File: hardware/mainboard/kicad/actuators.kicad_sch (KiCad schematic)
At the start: 14 parts, among them J5 J_SERVO1, J6 J_SERVO2, J7 J_SERVO3, J8 J_MOT, U7 DRV8833PWPR

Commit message: Platine rev B geroutet: alle 134 Footprints platziert, DRC ohne Fehler, 3 offene Verbindungen; Renders und Lagenbilder; Fertigervergleich
- Lagen: In1 GND, B.Cu geteilte Versorgungsflaeche GND_PWR/5V_SYS, Plane-Vias an jedem SMD-Pad
- Freerouting 2.5.0 (JAR, Temurin 25) mit zwei Nachlaeufen auf fixierter Verdrahtung und kollisionsgeprueften Stummeln
- check_design.py: Netzliste gegen Spezifikation §4 (OK), make.sh fuer die ganze Kette
- 3D-Modelle Teensy 4.1 und XT30PW-M (CadQuery), Renders und layers.pdf in kicad/img
- Fertiger_2026-10-21.md: JLCPCB empfohlen, Aisler als EU-Rueckfall, BMP390 bei JLC nicht lieferbar
- naechster Schritt laut kicad/README.md §8: Review-Punkte A1-A5 (review_kicad_2026-10-21.md) vor dem Handrouting

Co-Authored-By: Claude Opus 5.5 <noreply@anthropic.com>
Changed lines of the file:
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@@
 		(company "Mission Space")
 		(comment 1 "TVC-Servos am 2S-Akku, Fallschirm-Servo, Rollmotor DRV8833")
-		(comment 2 "erzeugt von hardware/mainboard/kicad/gen_schematic.py aus circuit.py - nicht von Hand aendern")
+		(comment 2 "erzeugt aus circuit.py (gen_schematic.py)")
 	)
 	(text "TVC-Servos am 2S-Akku, Fallschirm-Servo, Rollmotor DRV8833"
@@
 		(stroke (width 0) (type default))
 	)
-	(label "SERVO_YAW_S"
+	(global_label "SERVO_YAW_S"
+		(shape passive)
 		(at 26.67 64.77 270)
 		(fields_autoplaced yes)
-		(effects (font (size 1.27 1.27)) (justify right bottom))
+		(effects (font (size 1.27 1.27)) (justify right))
 	)
 	(symbol
@@
 		(stroke (width 0) (type default))
 	)
-	(label "SERVO_YAW_S"
+	(global_label "SERVO_YAW_S"
+		(shape passive)
 		(at 54.61 44.45 180)
 		(fields_autoplaced yes)
-		(effects (font (size 1.27 1.27)) (justify right bottom))
+		(effects (font (size 1.27 1.27)) (justify right))
 	)
 	(wire
@@
 		(stroke (width 0) (type default))
 	)
-	(label "SERVO_PITCH_S"
+	(global_label "SERVO_PITCH_S"
+		(shape passive)
 		(at 68.58 67.31 270)
 		(fields_autoplaced yes)
-		(effects (font (size 1.27 1.27)) (justify right bottom))
+		(effects (font (size 1.27 1.27)) (justify right))
 	)
 	(symbol
@@
 		(stroke (width 0) (type default))
 	)
-	(label "SERVO_PITCH_S"
+	(global_label "SERVO_PITCH_S"
+		(shape passive)
 		(at 99.06 44.45 180)
 		(fields_autoplaced yes)
-		(effects (font (size 1.27 1.27)) (justify right bottom))
+		(effects (font (size 1.27 1.27)) (justify right))
 	)
 	(wire
@@
 		(stroke (width 0) (type default))
 	)
-	(label "SERVO_CHUTE_S"
+	(global_label "SERVO_CHUTE_S"
+		(shape passive)
 		(at 114.3 67.31 270)
 		(fields_autoplaced yes)
-		(effects (font (size 1.27 1.27)) (justify right bottom))
+		(effects (font (size 1.27 1.27)) (justify right))
 	)
 	(symbol
@@
 		(stroke (width 0) (type default))
 	)
-	(label "SERVO_CHUTE_S"
+	(global_label "SERVO_CHUTE_S"
+		(shape passive)
 		(at 143.51 44.45 180)
 		(fields_autoplaced yes)
-		(effects (font (size 1.27 1.27)) (justify right bottom))
+		(effects (font (size 1.27 1.27)) (justify right))
 	)
 	(wire
@@
 		(stroke (width 0) (type default))
 	)
-	(label "U7_SLEEP"
+	(global_label "U7_SLEEP"
+		(shape passive)
 		(at 179.07 62.23 180)
 		(fields_autoplaced yes)
-		(effects (font (size 1.27 1.27)) (justify right bottom))
+		(effects (font (size 1.27 1.27)) (justify right))
 	)
 	(wire
@@
 		(stroke (width 0) (type default))
 	)
-	(label "MOT_A"
+	(global_label "MOT_A"
+		(shape passive)
 		(at 209.55 74.93 0)
 		(fields_autoplaced yes)
-		(effects (font (size 1.27 1.27)) (justify left bottom))
+		(effects (font (size 1.27 1.27)) (justify left))
 	)
 	(wire
@@
 		(stroke (width 0) (type default))
 	)
-	(label "MOT_B"
+	(global_label "MOT_B"
+		(shape passive)
 		(at 209.55 77.47 0)
 		(fields_autoplaced yes)
-		(effects (font (size 1.27 1.27)) (justify left bottom))
+		(effects (font (size 1.27 1.27)) (justify left))
 	)
 	(wire
@@
 		(stroke (width 0) (type default))
 	)
-	(label "MOT_B"
+	(global_label "MOT_B"
+		(shape passive)
 		(at 209.55 82.55 0)
 		(fields_autoplaced yes)
-		(effects (font (size 1.27 1.27)) (justify left bottom))
+		(effects (font (size 1.27 1.27)) (justify left))
 	)
 	(wire
@@
 		(stroke (width 0) (type default))
 	)
-	(label "MOT_A"
+	(global_label "MOT_A"
+		(shape passive)
 		(at 209.55 80.01 0)
 		(fields_autoplaced yes)
-		(effects (font (size 1.27 1.27)) (justify left bottom))
+		(effects (font (size 1.27 1.27)) (justify left))
 	)
 	(wire
@@
 		(stroke (width 0) (type default))
 	)
-	(label "U7_VCP"
+	(global_label "U7_VCP"
+		(shape passive)
 		(at 179.07 64.77 180)
 		(fields_autoplaced yes)
-		(effects (font (size 1.27 1.27)) (justify right bottom))
+		(effects (font (size 1.27 1.27)) (justify right))
 	)
 	(wire
@@
 		(stroke (width 0) (type default))
 	)
-	(label "U7_VINT"
+	(global_label "U7_VINT"
+		(shape passive)
 		(at 199.39 54.61 90)
 		(fields_autoplaced yes)
-		(effects (font (size 1.27 1.27)) (justify left bottom))
+		(effects (font (size 1.27 1.27)) (justify left))
 	)
 	(wire
@@
 		(stroke (width 0) (type default))
 	)
-	(label "U7_SLEEP"
+	(global_label "U7_SLEEP"
+		(shape passive)
 		(at 227.33 63.5 270)
 		(fields_autoplaced yes)
-		(effects (font (size 1.27 1.27)) (justify right bottom))
+		(effects (font (size 1.27 1.27)) (justify right))
 	)
 	(symbol
@@
 		(stroke (width 0) (type default))
 	)
-	(label "U7_VCP"
+	(global_label "U7_VCP"
+		(shape passive)
 		(at 294.64 48.26 90)
 		(fields_autoplaced yes)
-		(effects (font (size 1.27 1.27)) (justify left bottom))
+		(effects (font (size 1.27 1.27)) (justify left))
 	)
 	(wire
@@
 		(stroke (width 0) (type default))
 	)
-	(label "U7_VINT"
+	(global_label "U7_VINT"
+		(shape passive)
 		(at 170.18 115.57 90)
 		(fields_autoplaced yes)
-		(effects (font (size 1.27 1.27)) (justify left bottom))
+		(effects (font (size 1.27 1.27)) (justify left))
 	)
 	(wire
@@
 		(stroke (width 0) (type default))
 	)
-	(label "MOT_A"
+	(global_label "MOT_A"
+		(shape passive)
 		(at 191.77 109.22 180)
 		(fields_autoplaced yes)
-		(effects (font (size 1.27 1.27)) (justify right bottom))
+		(effects (font (size 1.27 1.27)) (justify right))
 	)
 	(wire
@@
 		(stroke (width 0) (type default))
 	)
-	(label "MOT_B"
+	(global_label "MOT_B"
+		(shape passive)
 		(at 191.77 111.76 180)
 		(fields_autoplaced yes)
-		(effects (font (size 1.27 1.27)) (justify right bottom))
+		(effects (font (size 1.27 1.27)) (justify right))
 	)
 	(rectangle
@@
 		(stroke (width 0) (type default))
 	)
-	(label "U7_VINT"
+	(global_label "U7_VINT"
+		(shape passive)
 		(at 318.77 44.45 270)
 		(fields_autoplaced yes)
-		(effects (font (size 1.27 1.27)) (justify right bottom))
+		(effects (font (size 1.27 1.27)) (justify right))
 	)
 	(embedded_fonts no)

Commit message: Kartonaut: Name, Missionsabzeichen, Bestückungsdruck neu, Lötstopp blau
- Projekt heißt Kartonaut (Karton + Astronaut); Flüge werden hochgezählt, Erstflug = Kartonaut 1
- Abzeichen als Polygone in hardware/mainboard/kicad/logo.py, SVGs in docs/brand/
- spacecode/ -> firmware/, Bodenstation-Repo groundcode -> kartonaut-ground (Links, .gitignore)
- gen_pcb.py silk: Bestückungsdruck nur neu setzen, auf der gerouteten Platine; 1,0 mm Schrift,
  freie Plätze statt Überlappungen, Kurznamen an den Steckern, Testpunkte mit Netznamen,
  kleines Abzeichen vorn; hinten Abzeichen 20 mm und Steckerbelegung
- Stackup JLC04161H-7628 mit blauem Lötstopp im Board, Renders mit Stackup-Farben
- DRC-Druckwarnungen 167 -> 14 (Rest aus Footprint-Umrissen)

Co-Authored-By: Claude Opus 5.5 <noreply@anthropic.com>
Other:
- company: Mission Space -> Kartonaut
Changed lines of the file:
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@@
 		(date "2026-10-21")
 		(rev "B")
-		(company "Mission Space")
+		(company "Kartonaut")
 		(comment 1 "TVC-Servos am 2S-Akku, Fallschirm-Servo, Rollmotor DRV8833")
 		(comment 2 "erzeugt aus circuit.py (gen_schematic.py)")

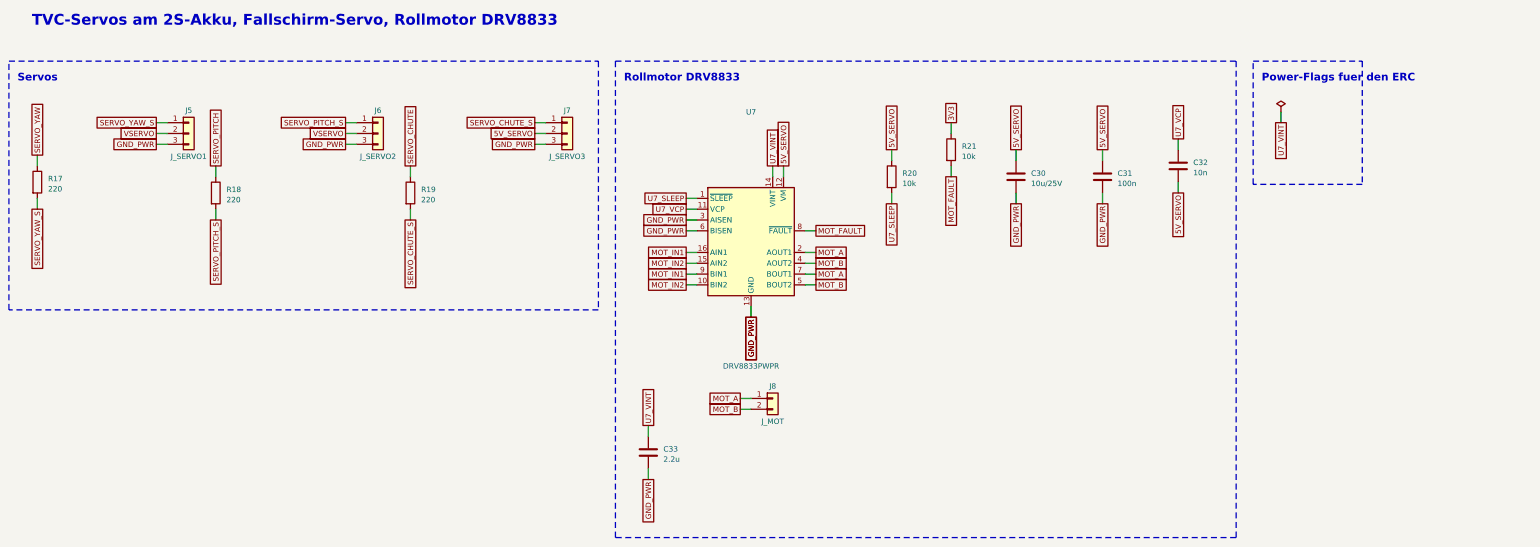
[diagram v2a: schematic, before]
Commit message: Mainboard rev B1: Review A1-A8 und Entscheidungen E1-E10 eingearbeitet, 2S-Pfad als F.Cu-Flaechen, 28 Verbindungen offen
Schaltung (circuit.py, ERC 0, Netzliste gegen README §4 OK): Hold-up hinter D1, EN-Teiler 330k/115k,
P-FET-Lastschalter je Akku, Polyfuse je Akku, Kelvin-Shunt mit INA239 an SPI1, BMP390 an SPI1,
74HC138/74HC4051 mit gemeinsamer Adresse, J_STACK 2x10 mit LDO 3V3_EXP, 1S-Lader MCP73831,
J_CHG2, vier Pyro-Kanaele (3/4 DNP), vierter Servo, alle Servos und Rollmotor an VSERVO,
3V3_SENS, eine WS2812B-Kette, Summer Pin 37, E22 NRST Pin 6; 166 Bauteile.

Platine (gen_pcb.py): neue Platzierung, 2S-Pfad, Pyro-Ausgaenge und VSYS_IN als F.Cu-Flaechen mit
Sperrflaechen fuer Freerouting, Strom-Klasse nur F.Cu, IMU-Zone 5 mm, patch mit Umweg ueber In2.
DRC 0 Fehler, Paritaet 0, kein 2S-Netz auf In2; 28 offene Verbindungen, Liste in kicad/README.md §5.5.
Spezifikation README.md und kicad/README.md auf B1 nachgezogen, review_check_layout.py fuer B1.

Co-Authored-By: Claude Opus 5.5 <noreply@anthropic.com>
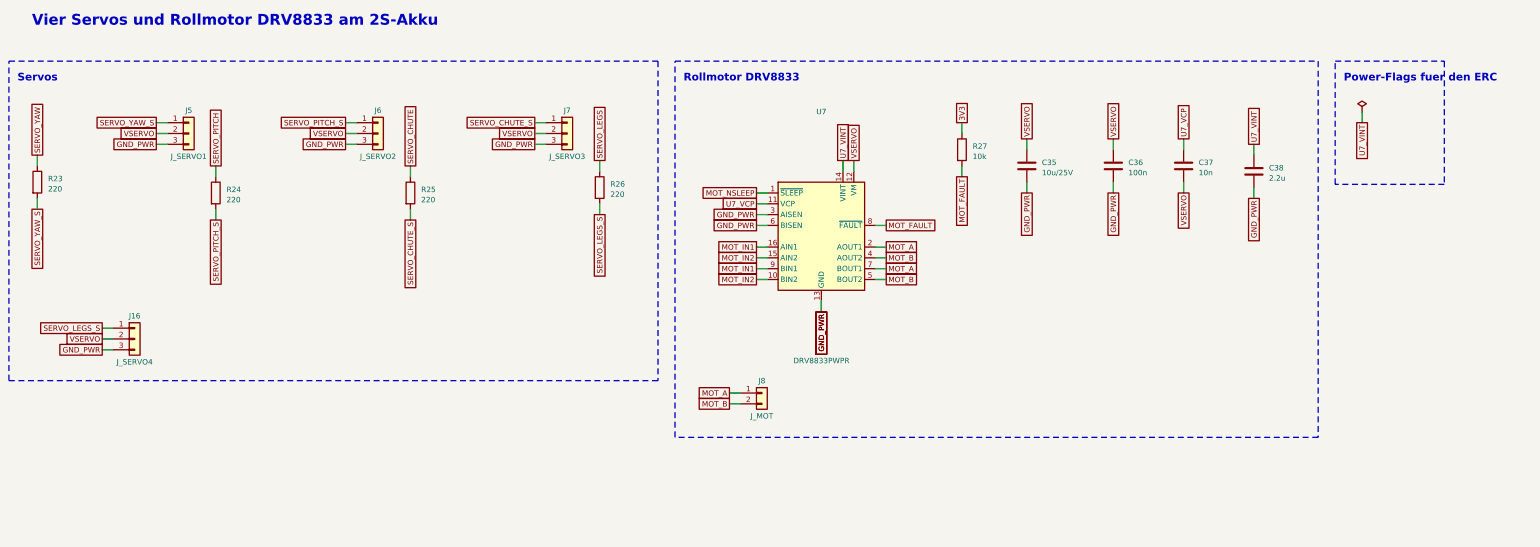
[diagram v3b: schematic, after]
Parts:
- removed C30: 10u/25V, Capacitor_SMD:C_0805_2012Metric, symbol Device:C
- removed C31: 100n, Capacitor_SMD:C_0603_1608Metric, symbol Device:C
- removed C32: 10n, Capacitor_SMD:C_0603_1608Metric, symbol Device:C
- removed C33: 2.2u, Capacitor_SMD:C_0603_1608Metric, symbol Device:C
- removed R17, R18, R19: 220, Resistor_SMD:R_0603_1608Metric, symbol Device:R
- removed R20, R21: 10k, Resistor_SMD:R_0603_1608Metric, symbol Device:R
- added C35: 10u/25V, Capacitor_SMD:C_0805_2012Metric, symbol Device:C
- added C36: 100n, Capacitor_SMD:C_0603_1608Metric, symbol Device:C
- added C37: 10n, Capacitor_SMD:C_0603_1608Metric, symbol Device:C
- added C38: 2.2u, Capacitor_SMD:C_0603_1608Metric, symbol Device:C
- added J16: J_SERVO4, Connector_JST:JST_XH_B3B-XH-A_1x03_P2.50mm_Vertical, symbol Connector_Generic:Conn_01x03
- added R23, R24, R25, R26: 220, Resistor_SMD:R_0603_1608Metric, symbol Device:R
- added R27: 10k, Resistor_SMD:R_0603_1608Metric, symbol Device:R
- J8: footprint Connector_JST:JST_PH_B2B-PH-K_1x02_P2.00mm_Vertical -> Connector_JST:JST_XH_B2B-XH-A_1x02_P2.50mm_Vertical
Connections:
- net 5V_SERVO is gone; now on net VSERVO: J7.2 (Pin_2), U7.12 (VM)
- net 3V3: now also R27.1
- net GND_PWR: now also C35.2, C36.2, C38.2, J16.3 (Pin_3)
- net MOT_FAULT: now also R27.2
- net SERVO_CHUTE: now also R25.1
- net SERVO_CHUTE_S: now also R25.2
- net SERVO_PITCH: now also R24.1
- net SERVO_PITCH_S: now also R24.2
- net SERVO_YAW: now also R23.1
- net SERVO_YAW_S: now also R23.2
- net U7_VCP: now also C37.1
- net U7_VINT: now also C38.1
- net VSERVO: now also C35.1, C36.1, C37.2, J16.2 (Pin_2)
- net U7_SLEEP renamed MOT_NSLEEP
- new net SERVO_LEGS: R26.1
- new net SERVO_LEGS_S: J16.1 (Pin_1), R26.2
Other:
- note added: "Vier Servos und Rollmotor DRV8833 am 2S-Akku"
- note removed: "TVC-Servos am 2S-Akku, Fallschirm-Servo, Rollmotor DRV8833"
- moved on the sheet: J8, U7
